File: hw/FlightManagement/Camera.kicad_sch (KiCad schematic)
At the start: 1 part, among them J5 Conn_01x24_MountingPin

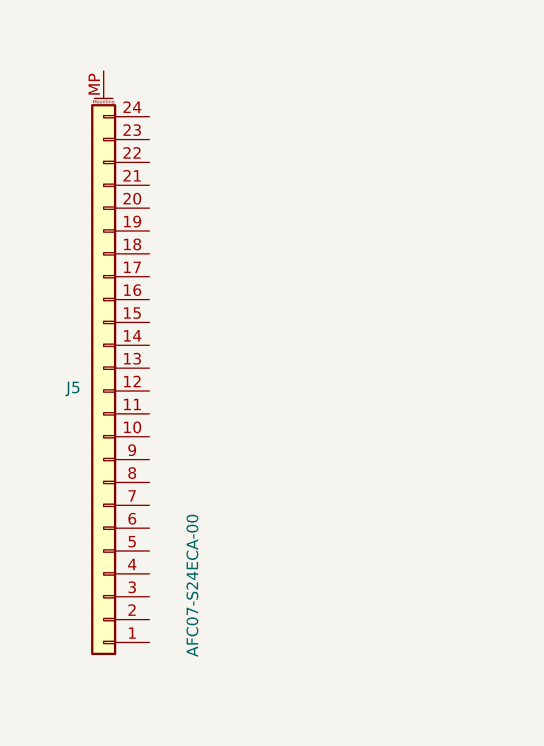
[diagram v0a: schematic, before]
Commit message: final FC placement
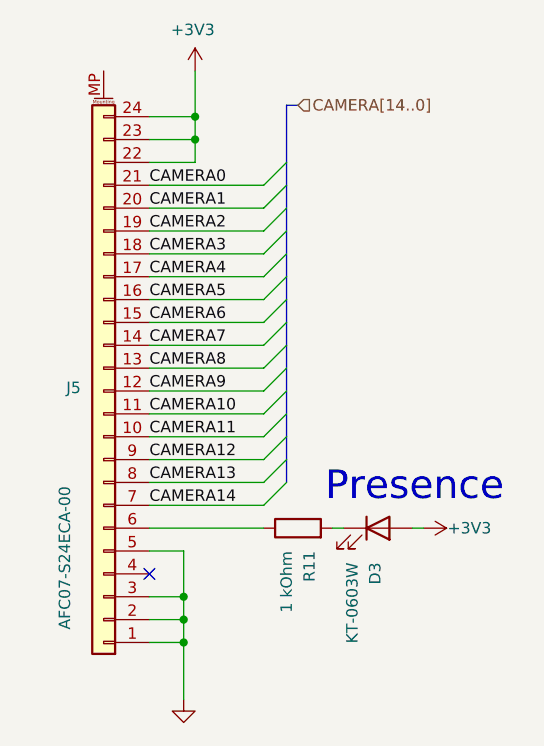
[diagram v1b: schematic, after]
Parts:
- added D3: KT-0603W, LED_SMD:LED_0603_1608Metric_Pad1.05x0.95mm_HandSolder, symbol Device:LED
- added R11: 1 kOhm, Resistor_SMD:R_0603_1608Metric_Pad0.98x0.95mm_HandSolder, symbol Device:R
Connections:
- net GND: now reaches J5.1 (Pin_1)
- net GND: now also J5.2 (Pin_2), J5.3 (Pin_3), J5.5 (Pin_5)
- net CAMERA11: now reaches J5.10 (Pin_10)
- net CAMERA10: now reaches J5.11 (Pin_11)
- net CAMERA9: now reaches J5.12 (Pin_12)
- net CAMERA8: now reaches J5.13 (Pin_13)
- net CAMERA7: now reaches J5.14 (Pin_14)
- net CAMERA6: now reaches J5.15 (Pin_15)
- net CAMERA5: now reaches J5.16 (Pin_16)
- net CAMERA4: now reaches J5.17 (Pin_17)
- net CAMERA3: now reaches J5.18 (Pin_18)
- net CAMERA2: now reaches J5.19 (Pin_19)
- net CAMERA1: now reaches J5.20 (Pin_20)
- net CAMERA0: now reaches J5.21 (Pin_21)
- net +3V3: now reaches J5.22 (Pin_22)
- net +3V3: now also J5.23 (Pin_23), J5.24 (Pin_24), D3.2 (A)
- net at J5.6 (Pin_6): now also R11.1
- net CAMERA14: now reaches J5.7 (Pin_7)
- net CAMERA13: now reaches J5.8 (Pin_8)
- net CAMERA12: now reaches J5.9 (Pin_9)
- new net: D3.1 (K), R11.2
- no-connect marks 0 -> 1
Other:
- note added: "Presence"

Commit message: finish fmu routing
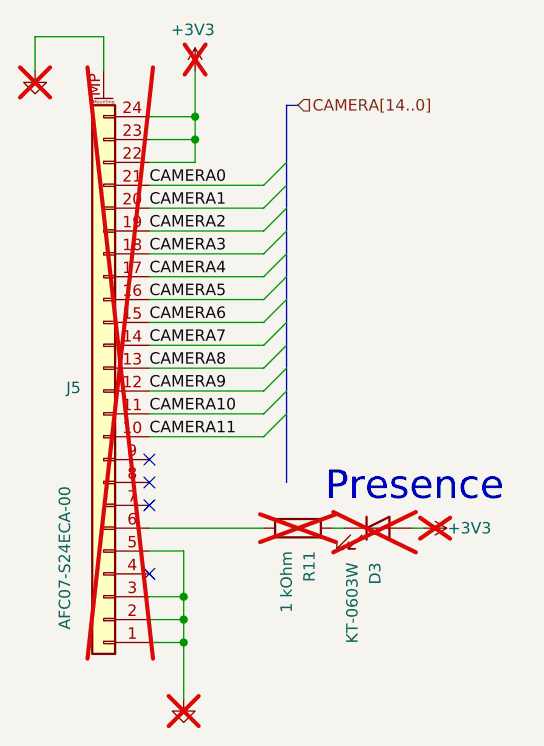
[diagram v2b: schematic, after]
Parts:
- D3, J5, R11: now not fitted; now left out of the parts list
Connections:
- net GND: now also J5.MP (MountPin)
- net CAMERA12: no longer names the net of J5.9 (Pin_9)
- net CAMERA13: no longer names the net of J5.8 (Pin_8)
- net CAMERA14: no longer names the net of J5.7 (Pin_7)
- no-connect marks 1 -> 4
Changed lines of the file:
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@@
+	)
+	(no_connect
+		(at 33.02 69.85)
+	)
+	(no_connect
+		(at 33.02 67.31)
 	)
 	(no_connect
 		(at 33.02 77.47)
 	)
+	(no_connect
+		(at 33.02 64.77)
+	)
 	(bus_entry
 		(at 48.26 44.45)
@@
 	)
 	(bus_entry
-		(at 48.26 62.23)
-		(size -2.54 2.54)
-		(stroke
-			(width 0)
-			(type default)
-		)
-	)
-	(bus_entry
 		(at 48.26 31.75)
 		(size -2.54 2.54)
@@
 	)
 	(bus_entry
-		(at 48.26 67.31)
-		(size -2.54 2.54)
-		(stroke
-			(width 0)
-			(type default)
-		)
-	)
-	(bus_entry
-		(at 48.26 64.77)
-		(size -2.54 2.54)
-		(stroke
-			(width 0)
-			(type default)
-		)
-	)
-	(bus_entry
 		(at 48.26 39.37)
 		(size -2.54 2.54)
@@
 	(bus
 		(pts
-			(xy 48.26 59.69) (xy 48.26 62.23)
+			(xy 48.26 59.69) (xy 48.26 67.31)
 		)
 		(stroke
@@
 		)
 	)
+	(wire
+		(pts
+			(xy 20.32 21.59) (xy 20.32 17.78)
+		)
+		(stroke
+			(width 0)
+			(type default)
+		)
+	)
 	(bus
 		(pts
@@
 		)
 	)
-	(bus
-		(pts
-			(xy 48.26 64.77) (xy 48.26 67.31)
-		)
-		(stroke
-			(width 0)
-			(type default)
-		)
-	)
 	(wire
 		(pts
@@
 		)
 	)
-	(bus
-		(pts
-			(xy 48.26 62.23) (xy 48.26 64.77)
-		)
-		(stroke
-			(width 0)
-			(type default)
-		)
-	)
 	(wire
 		(pts
@@
 	(wire
 		(pts
-			(xy 33.02 69.85) (xy 45.72 69.85)
-		)
-		(stroke
-			(width 0)
-			(type default)
-		)
-	)
-	(wire
-		(pts
 			(xy 45.72 41.91) (xy 33.02 41.91)
 		)
@@
 	(wire
 		(pts
-			(xy 33.02 64.77) (xy 45.72 64.77)
-		)
-		(stroke
-			(width 0)
-			(type default)
-		)
-	)
-	(wire
-		(pts
 			(xy 33.02 57.15) (xy 45.72 57.15)
 		)
@@
 	(wire
 		(pts
+			(xy 20.32 17.78) (xy 27.94 17.78)
+		)
+		(stroke
+			(width 0)
+			(type default)
+		)
+	)
+	(wire
+		(pts
 			(xy 33.02 82.55) (xy 36.83 82.55)
 		)
@@
 		)
 	)
-	(wire
-		(pts
-			(xy 33.02 67.31) (xy 45.72 67.31)
-		)
-		(stroke
-			(width 0)
-			(type default)
-		)
-	)
 	(bus
 		(pts
@@
 		(pts
 			(xy 33.02 29.21) (xy 38.1 29.21)
+		)
+		(stroke
+			(width 0)
+			(type default)
+		)
+	)
+	(wire
+		(pts
+			(xy 27.94 17.78) (xy 27.94 21.59)
 		)
 		(stroke
@@
 		)
 	)
-	(label "CAMERA13"
-		(at 33.02 67.31 0)
-		(effects
-			(font
-				(size 1.27 1.27)
-			)
-			(justify left bottom)
-		)
-	)
 	(label "CAMERA1"
 		(at 33.02 36.83 0)
@@
 	(label "CAMERA10"
 		(at 33.02 59.69 0)
-		(effects
-			(font
-				(size 1.27 1.27)
-			)
-			(justify left bottom)
-		)
-	)
-	(label "CAMERA14"
-		(at 33.02 69.85 0)
-		(effects
-			(font
-				(size 1.27 1.27)
-			)
-			(justify left bottom)
-		)
-	)
-	(label "CAMERA12"
-		(at 33.02 64.77 0)
 		(effects
 			(font
@@
 			)
 			(justify left)
+		)
+	)
+	(symbol
+		(lib_id "power:GND")
+		(at 20.32 21.59 0)
+		(unit 1)
+		(exclude_from_sim no)
+		(in_bom no)
+		(on_board no)
+		(dnp yes)
+		(fields_autoplaced yes)
+		(property "Reference" "#PWR099"
+			(at 20.32 27.94 0)
+			(effects
+				(font
+					(size 1.27 1.27)
+				)
+				(hide yes)
+			)
+		)
+		(property "Value" "GND"
+			(at 20.32 26.67 0)
+			(effects
+				(font
+					(size 1.27 1.27)
+				)
+				(hide yes)
+			)
+		)
+		(property "Footprint" ""
+			(at 20.32 21.59 0)
+			(effects
+				(font
+					(size 1.27 1.27)
+				)
+				(hide yes)
+			)
+		)
+		(property "Datasheet" ""
+			(at 20.32 21.59 0)
+			(effects
+				(font
+					(size 1.27 1.27)
+				)
+				(hide yes)
+			)
+		)
+		(property "Description" "Power symbol creates a global label with name \"GND\" , ground"
+			(at 20.32 21.59 0)
+			(effects
+				(font
+					(size 1.27 1.27)
+				)
+				(hide yes)
+			)
+		)
+		(pin "1"
+		)
+		(instances
+			(project "FlightManagement"
+				(path "/428dbf80-1251-4f56-8786-11b9f3c75d18/98f1eb1c-f9f2-4688-9085-59621c0d46c9"
+					(reference "#PWR099")
+					(unit 1)
+				)
+			)
 		)
 	)
@@
 		(unit 1)
 		(exclude_from_sim no)
-		(in_bom yes)
-		(on_board yes)
-		(dnp no)
+		(in_bom no)
+		(on_board no)
+		(dnp yes)
 		(property "Reference" "#PWR073"
 			(at 38.1 25.4 0)
@@
 		(unit 1)
 		(exclude_from_sim no)
-		(in_bom yes)
-		(on_board yes)
-		(dnp no)
+		(in_bom no)
+		(on_board no)
+		(dnp yes)
 		(fields_autoplaced yes)
 		(property "Reference" "#PWR090"
@@
 		(unit 1)
 		(exclude_from_sim no)
-		(in_bom yes)
-		(on_board yes)
-		(dnp no)
+		(in_bom no)
+		(on_board no)
+		(dnp yes)
 		(fields_autoplaced yes)
 		(property "Reference" "D3"
@@
 		(unit 1)
 		(exclude_from_sim no)
-		(in_bom yes)
-		(on_board yes)
-		(dnp no)
+		(in_bom no)
+		(on_board no)
+		(dnp yes)
 		(fields_autoplaced yes)
 		(property "Reference" "R11"
@@
 		(unit 1)
 		(exclude_from_sim no)
-		(in_bom yes)
-		(on_board yes)
-		(dnp no)
+		(in_bom no)
+		(on_board no)
+		(dnp yes)
 		(property "Reference" "#PWR091"
 			(at 59.69 72.39 0)
@@
 		(unit 1)
 		(exclude_from_sim no)
-		(in_bom yes)
-		(on_board yes)
-		(dnp no)
+		(in_bom no)
+		(on_board no)
+		(dnp yes)
 		(property "Reference" "J5"
 			(at 25.4 56.7945 0)

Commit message: start working on firmware
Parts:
- renumbered D3 to D5, J5 to J7, R11 to R23
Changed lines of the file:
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@@
 		(dnp yes)
 		(fields_autoplaced yes)
-		(property "Reference" "#PWR099"
+		(property "Reference" "#PWR0113"
 			(at 20.32 27.94 0)
 			(effects
@@
 			(project "FlightManagement"
 				(path "/428dbf80-1251-4f56-8786-11b9f3c75d18/98f1eb1c-f9f2-4688-9085-59621c0d46c9"
-					(reference "#PWR099")
+					(reference "#PWR0113")
 					(unit 1)
 				)
@@
 		(on_board no)
 		(dnp yes)
-		(property "Reference" "#PWR073"
+		(property "Reference" "#PWR0114"
 			(at 38.1 25.4 0)
 			(effects
@@
 			(project "FlightManagement"
 				(path "/428dbf80-1251-4f56-8786-11b9f3c75d18/98f1eb1c-f9f2-4688-9085-59621c0d46c9"
-					(reference "#PWR073")
+					(reference "#PWR0114")
 					(unit 1)
 				)
@@
 		(dnp yes)
 		(fields_autoplaced yes)
-		(property "Reference" "#PWR090"
+		(property "Reference" "#PWR0116"
 			(at 36.83 97.79 0)
 			(effects
@@
 			(project "FlightManagement"
 				(path "/428dbf80-1251-4f56-8786-11b9f3c75d18/98f1eb1c-f9f2-4688-9085-59621c0d46c9"
-					(reference "#PWR090")
+					(reference "#PWR0116")
 					(unit 1)
 				)
@@
 		(dnp yes)
 		(fields_autoplaced yes)
-		(property "Reference" "D3"
+		(property "Reference" "D5"
 			(at 58.1026 76.2 90)
 			(effects
@@
 			(project "FlightManagement"
 				(path "/428dbf80-1251-4f56-8786-11b9f3c75d18/98f1eb1c-f9f2-4688-9085-59621c0d46c9"
-					(reference "D3")
+					(reference "D5")
 					(unit 1)
 				)
@@
 		(dnp yes)
 		(fields_autoplaced yes)
-		(property "Reference" "R11"
+		(property "Reference" "R23"
 			(at 50.8001 74.93 0)
 			(effects
@@
 			(project "FlightManagement"
 				(path "/428dbf80-1251-4f56-8786-11b9f3c75d18/98f1eb1c-f9f2-4688-9085-59621c0d46c9"
-					(reference "R11")
+					(reference "R23")
 					(unit 1)
 				)
@@
 		(on_board no)
 		(dnp yes)
-		(property "Reference" "#PWR091"
+		(property "Reference" "#PWR0115"
 			(at 59.69 72.39 0)
 			(effects
@@
 			(project "FlightManagement"
 				(path "/428dbf80-1251-4f56-8786-11b9f3c75d18/98f1eb1c-f9f2-4688-9085-59621c0d46c9"
-					(reference "#PWR091")
+					(reference "#PWR0115")
 					(unit 1)
 				)
@@
 		(on_board no)
 		(dnp yes)
-		(property "Reference" "J5"
+		(property "Reference" "J7"
 			(at 25.4 56.7945 0)
 			(effects
@@
 			(project "FlightManagement"
 				(path "/428dbf80-1251-4f56-8786-11b9f3c75d18/98f1eb1c-f9f2-4688-9085-59621c0d46c9"
-					(reference "J5")
-					(unit 1)
-				)
+					(reference "J7")
+					(unit 1)
+				)
